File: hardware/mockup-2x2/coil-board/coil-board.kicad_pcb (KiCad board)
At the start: 4 copper layers, 100 x 100 mm, 25 parts, among them J1 COIL_JOINT_1x12, M1 NPTH, M2 NPTH, M3 NPTH, M4 NPTH

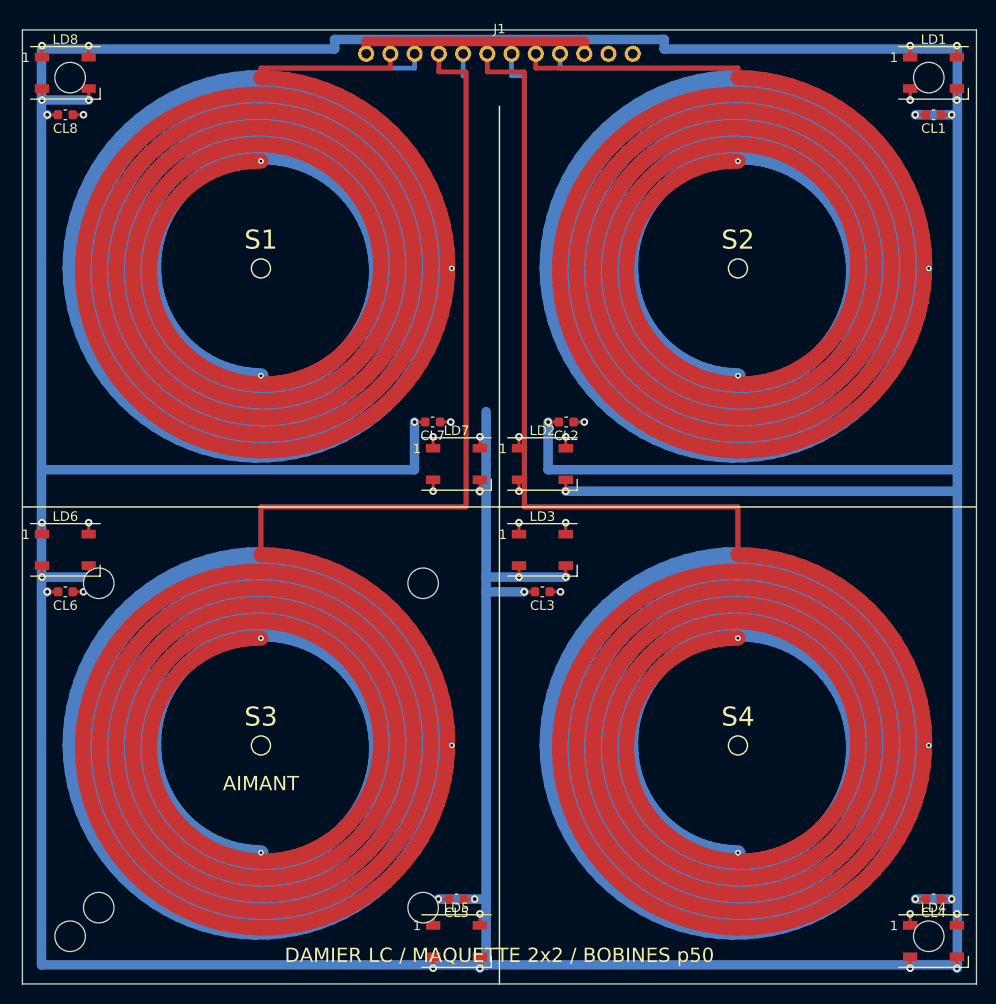
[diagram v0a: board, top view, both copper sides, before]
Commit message: Pilote simple : la carte bobines 100 x 100 passive, fermée et commandable
Demande du 07/10 : un pilote au minimum de composants, dans le palier
100 x 100, une seule carte à concevoir, le traitement sur un shield
soudé à la main à côté de la Nucleo. C'est la maquette de l'ADR 0008
sans ses LED.

- `mockup.coil_board.leds.fitted` dans le yaml : false coupe les LED de
  camp et leur chaîne ; coilgen ne les pose plus, la nomenclature et le
  placement n'ont plus que leur en-tête, les tests suivent le yaml.
- La bande de masse du connecteur passait sur les pastilles des broches
  2 à 9 (seize défauts) : elle court au bord, en 0,5 mm, et le build
  vérifie la cote. Repère J1 rentré dans la carte, lignes de cases à
  1 mm du bord, texte de sérigraphie PILOTE 2x2.
- DRC KiCad zéro, zéro élément non connecté, gerbers et empreinte
  commités ; fabcheck la déclare commandable, le test d'audit la compte
  parmi les cartes nues.
- Fiche du pilote (docs/bom-pilote.md) : ce qu'il réunit, trois options
  de shield, 130 à 195 EUR TTC tout compris avec la carte analogique
  existante soudée à la main ; le modèle prédit 0,12 à 0,74 V crête sur
  la spirale, première mesure à faire avant de souder le shield.
- README de la carte, README de la maquette, notes 07, 09, 22 et 23,
  index de la documentation.
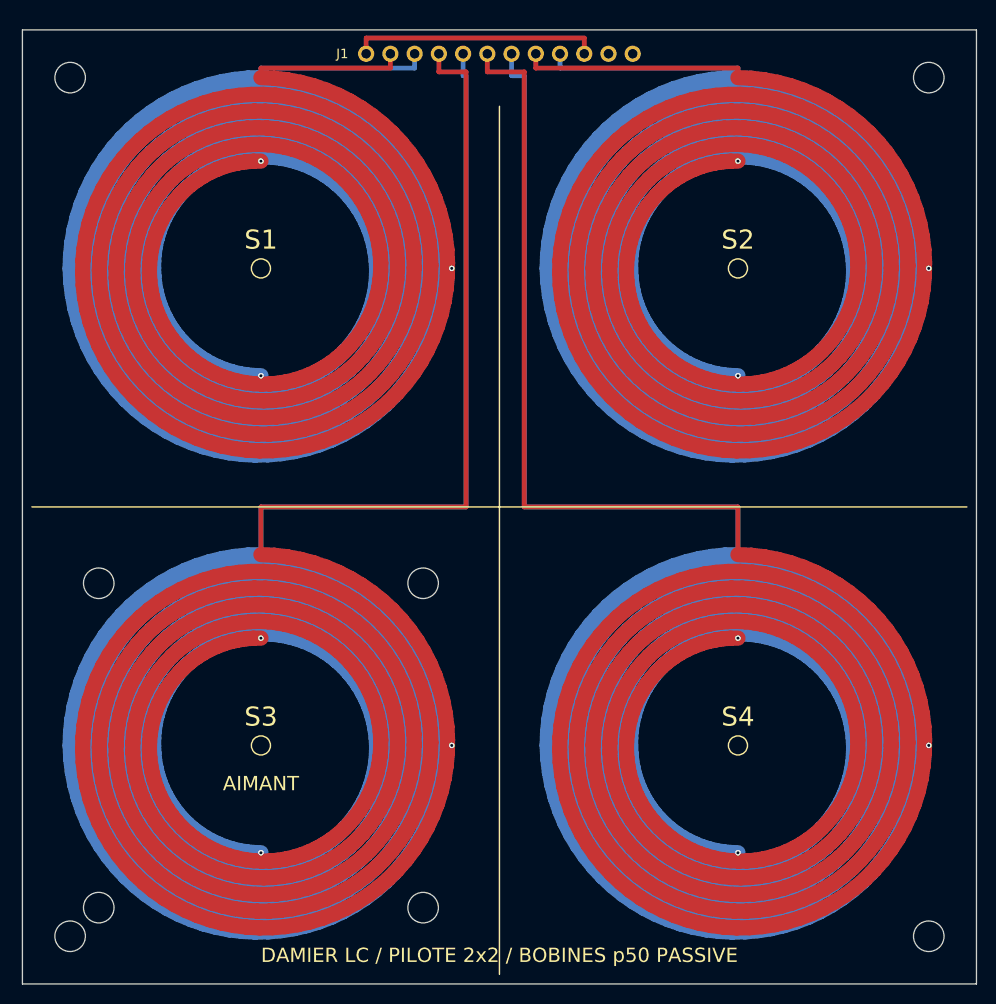
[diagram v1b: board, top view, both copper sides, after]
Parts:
- removed CL1, CL2, CL3, CL4, CL5, CL6, CL7, CL8: 100n, Capacitor_SMD:C_0603_1608Metric
- removed LD1, LD2, LD3, LD4, LD5, LD6, LD7, LD8: WS2812B, LED_SMD:LED_WS2812B_PLCC4_5.0x5.0mm_P3.2mm
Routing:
- net LED_5V: track 641.5 -> 0.00 mm, vias 16 -> 0
- net GND: track 659.5 -> 26.2 mm, vias 16 -> 0
- net LED_L7: track 99.8 -> 0.00 mm, vias 2 -> 0
- net LED_L5: track 93.7 -> 0.00 mm, vias 2 -> 0
- net LED_L3: track 91.1 -> 0.00 mm, vias 2 -> 0
- net LED_L1: track 87.4 -> 0.00 mm, vias 2 -> 0
- net LED_L6: track 65.3 -> 0.00 mm, vias 2 -> 0
- net LED_L4: track 53.3 -> 0.00 mm, vias 2 -> 0
- net LED_DIN: track 42.8 -> 0.00 mm, vias 1 -> 0
- net LED_L2: track 10.6 -> 0.00 mm, vias 2 -> 0
- net LED_END: track 1.20 -> 0.00 mm, vias 1 -> 0
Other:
- board text added: "DAMIER LC / PILOTE 2x2 / BOBINES p50 PASSIVE"
- board text removed: "DAMIER LC / MAQUETTE 2x2 / BOBINES p50"
